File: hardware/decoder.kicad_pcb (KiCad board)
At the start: 4 copper layers, 20.7 x 10.8 mm, 24 parts, among them J1 Conn_PluX16, J2 Conn_01x05, Q1 DTC144EETL, Q2 PUMH10, Q3 PUMH10, Q4 PUMH10, U1 XC6206P332MR, U2 STM32L031G6Ux, U3 DRV8872

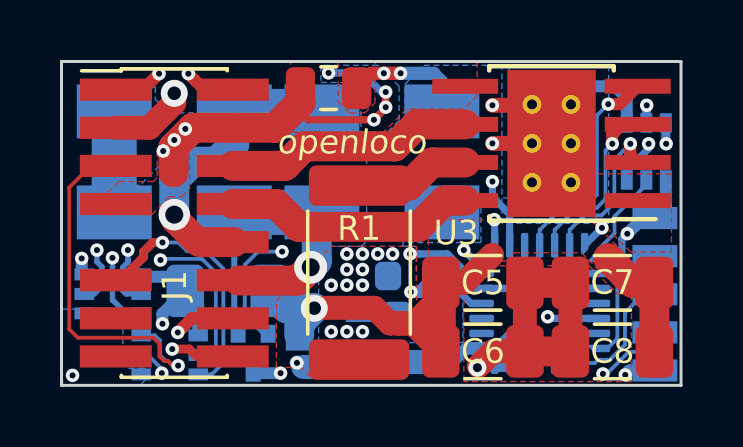
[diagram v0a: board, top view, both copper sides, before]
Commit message: Corrected 3V3 pad of µC too big (caused solder bridges with next pad)
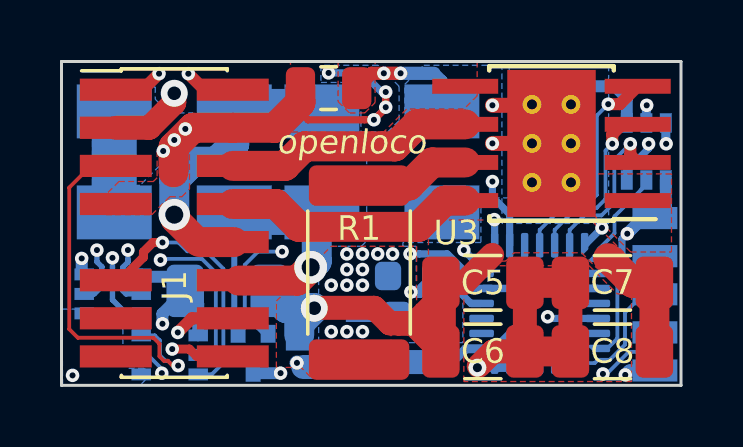
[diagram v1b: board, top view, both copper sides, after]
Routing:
- removed copper zone on B.Cu, net +3V3
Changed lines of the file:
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@@
   )
   (layers
-    (0 F.Cu signal hide)
-    (1 In1.Cu signal hide)
-    (2 In2.Cu signal hide)
+    (0 F.Cu signal)
+    (1 In1.Cu signal)
+    (2 In2.Cu signal)
     (31 B.Cu signal)
     (32 B.Adhes user hide)
@@
     (34 B.Paste user hide)
     (35 F.Paste user hide)
-    (36 B.SilkS user)
+    (36 B.SilkS user hide)
     (37 F.SilkS user hide)
     (38 B.Mask user hide)
@@
   )
   (setup
-    (last_trace_width 0.127)
+    (last_trace_width 0.3)
     (user_trace_width 0.127)
     (user_trace_width 0.135)
     (user_trace_width 0.2)
     (user_trace_width 0.24)
+    (user_trace_width 0.3)
     (user_trace_width 0.4)
-    (user_trace_width 0.5)
     (user_trace_width 0.8)
     (user_trace_width 1)
@@
   (segment (start 150.9593 96.4645) (end 150.4468 96.4645) (width 0.25) (layer B.Cu) (net 3))
   (segment (start 141.0691 99.0829) (end 140.9319 98.9457) (width 0.5) (layer B.Cu) (net 3))
-  (segment (start 146.5718 98.4645) (end 146.1159 98.9204) (width 0.4) (layer B.Cu) (net 3))
-  (segment (start 146.1159 98.9204) (end 145.5293 98.9204) (width 0.4) (layer B.Cu) (net 3))
-  (segment (start 147.21078 98.4645) (end 146.74828 98.4645) (width 0.4) (layer B.Cu) (net 3))
-  (segment (start 147.0343 98.4645) (end 146.5718 98.4645) (width 0.4) (layer B.Cu) (net 3))
   (segment (start 148.59 97.3885) (end 147.744 98.2345) (width 0.24) (layer B.Cu) (net 3))
   (segment (start 148.59 96.4645) (end 148.59 97.3885) (width 0.24) (layer B.Cu) (net 3))
-  (segment (start 147.744 98.2345) (end 147.193 98.4885) (width 0.24) (layer B.Cu) (net 3))
   (segment (start 141.250098 98.9457) (end 140.9319 98.9457) (width 0.15) (layer In1.Cu) (net 3))
   (segment (start 144.058519 98.237119) (end 143.349938 98.9457) (width 0.15) (layer In1.Cu) (net 3))
@@
   (segment (start 146.241899 96.0755) (end 144.617398 96.0755) (width 0.15) (layer In1.Cu) (net 3))
   (segment (start 144.617398 96.0755) (end 144.05852 96.634378) (width 0.15) (layer In1.Cu) (net 3))
+  (segment (start 146.1159 98.9204) (end 145.5293 98.9204) (width 0.3) (layer B.Cu) (net 3))
+  (segment (start 146.5605 98.4758) (end 146.1159 98.9204) (width 0.3) (layer B.Cu) (net 3))
+  (segment (start 146.5605 98.4758) (end 147.204156 98.4758) (width 0.3) (layer B.Cu) (net 3))
+  (segment (start 147.744 98.2345) (end 147.32 98.429956) (width 0.24) (layer B.Cu) (net 3))
+  (segment (start 147.32 98.429956) (end 147.193 98.4885) (width 0.24) (layer B.Cu) (net 3))
   (via (at 144.7292 96.5835) (size 0.45) (drill 0.2) (layers F.Cu B.Cu) (net 4))
   (via (at 151.13 99.314) (size 0.45) (drill 0.2) (layers F.Cu B.Cu) (net 4))
@@
       )
     )
-  )
-  (zone (net 3) (net_name +3V3) (layer B.Cu) (hatch edge 0.508)
-    (connect_pads yes (clearance 0.1))
-    (min_thickness 0.11)
-    (fill yes (arc_segments 32) (thermal_gap 0.1) (thermal_bridge_width 0.5))
-    (polygon
-      (pts
-        (xy 147.12442 98.26498) (xy 147.40128 98.26498) (xy 147.48764 98.35134) (xy 147.48764 98.47072) (xy 147.2946 98.66376)
-        (xy 147.12442 98.66376)
-      )
-    )
